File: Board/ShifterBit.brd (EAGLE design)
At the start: 27.2 x 51.2 mm, 10 parts

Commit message: renamed and added voltage divider for signal input
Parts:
- added R4: 2200, SparkFun-Passives:0603-RES
- added R5: 560, SparkFun-Passives:0603-RES
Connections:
- net A: now also R4.1, R5.2
- net GND: now also R5.1
- net SIG_IN: now also R4.2
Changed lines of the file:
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@@
 <element name="R2" library="SparkFun-Passives" package="0603-RES" value="56" x="9.3" y="50.8"/>
 <element name="R3" library="SparkFun-Passives" package="0603-RES" value="56" x="9.1" y="7.4"/>
+<element name="R4" library="SparkFun-Passives" package="0603-RES" value="2200" x="22.1" y="44.6"/>
+<element name="R5" library="SparkFun-Passives" package="0603-RES" value="560" x="18.4" y="44.6"/>
 </elements>
 <signals>
@@
 <contactref element="LED1" pad="C"/>
 <contactref element="LED2" pad="C"/>
+<contactref element="R5" pad="1"/>
 <wire x1="11.45" y1="53.13" x2="10.67" y2="56.835" width="0" layer="19" extent="16-16"/>
 <wire x1="14.177" y1="50.8" x2="11.45" y2="53.13" width="0" layer="19" extent="1-16"/>
@@
 <wire x1="6.5" y1="24.15" x2="6.6" y2="32.1" width="0" layer="19" extent="16-16"/>
 <wire x1="2.8" y1="17.77" x2="6.5" y2="24.15" width="0" layer="19" extent="16-16"/>
-<wire x1="13.777" y1="7.3" x2="2.8" y2="17.77" width="0" layer="19" extent="1-1"/>
+<wire x1="18.8" y1="22.25" x2="6.5" y2="24.15" width="0" layer="19" extent="16-16"/>
+<wire x1="23.2" y1="16.67" x2="18.8" y2="22.25" width="0" layer="19" extent="16-16"/>
+<wire x1="13.777" y1="7.3" x2="23.2" y2="16.67" width="0" layer="19" extent="1-1"/>
 <wire x1="10.67" y1="3.44" x2="13.777" y2="7.3" width="0" layer="19" extent="1-1"/>
-<wire x1="23.2" y1="16.67" x2="13.777" y2="7.3" width="0" layer="19" extent="1-1"/>
-<wire x1="18.8" y1="22.25" x2="23.2" y2="16.67" width="0" layer="19" extent="16-16"/>
+<wire x1="17.55" y1="44.6" x2="10.67" y2="3.44" width="0" layer="19" extent="1-1"/>
 </signal>
 <signal name="VCC">
@@
 <contactref element="BSM1" pad="SIG1"/>
 <contactref element="R1" pad="2"/>
+<contactref element="R4" pad="2"/>
 <wire x1="13.15" y1="53.13" x2="13.21" y2="56.835" width="0" layer="19" extent="16-16"/>
+<wire x1="22.95" y1="44.6" x2="13.15" y2="53.13" width="0" layer="19" extent="1-16"/>
 </signal>
 <signal name="RST">
@@
 <signal name="A">
 <contactref element="P1" pad="2"/>
+<contactref element="R5" pad="2"/>
+<contactref element="R4" pad="1"/>
+<wire x1="21.25" y1="44.6" x2="23.2" y2="36.99" width="0" layer="19" extent="1-1"/>
+<wire x1="19.25" y1="44.6" x2="21.25" y2="44.6" width="0" layer="19" extent="1-1"/>
 </signal>
 <signal name="EN">

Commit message: added transistor and some labels
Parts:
- added Q1: (no value), SparkFun-DiscreteSemi:TO-92-AMMO
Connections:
- new net N$14: Q1.3
- net D16: now also Q1.2
- net VCC: now also Q1.1
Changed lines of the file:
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@@
 <element name="R4" library="SparkFun-Passives" package="0603-RES" value="2200" x="22.1" y="44.6"/>
 <element name="R5" library="SparkFun-Passives" package="0603-RES" value="560" x="18.4" y="44.6"/>
+<element name="Q1" library="SparkFun-DiscreteSemi" package="TO-92-AMMO" value="" x="-0.4" y="-22.5"/>
 </elements>
 <signals>
@@
 <contactref element="BSM1" pad="VCC1"/>
 <contactref element="BSF1" pad="VCC"/>
+<contactref element="Q1" pad="1"/>
 <wire x1="15.75" y1="3.44" x2="15.75" y2="56.835" width="0" layer="19" extent="1-1"/>
+<wire x1="-2.94" y1="-22.5" x2="15.75" y2="3.44" width="0" layer="19" extent="1-1"/>
 </signal>
 <signal name="SIG_OUT">
@@
 <signal name="D16">
 <contactref element="P1" pad="4"/>
+<contactref element="Q1" pad="2"/>
+<wire x1="-0.4" y1="-22.5" x2="23.2" y2="31.91" width="0" layer="19" extent="1-1"/>
 </signal>
 <signal name="D14">
@@
 <wire x1="12.023" y1="7.3" x2="9.95" y2="7.4" width="0" layer="19" extent="1-1"/>
 </signal>
+<signal name="N$14">
+<contactref element="Q1" pad="3"/>
+</signal>
 </signals>

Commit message: added resistor to dac
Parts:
- added R6: 1200, SparkFun-Resistors:0603-RES
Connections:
- new net N$10: Q1.2, R6.2
- net D16: now also R6.1; no longer Q1.2
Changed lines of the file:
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@@
 <layer number="227" name="227bmp" color="7" fill="1" visible="yes" active="yes"/>
 <layer number="228" name="228bmp" color="7" fill="1" visible="yes" active="yes"/>
+<layer number="229" name="229bmp" color="7" fill="1" visible="yes" active="yes"/>
+<layer number="230" name="230bmp" color="7" fill="1" visible="yes" active="yes"/>
 <layer number="231" name="Eagle3D_PG1" color="7" fill="1" visible="no" active="no"/>
 <layer number="232" name="Eagle3D_PG2" color="7" fill="1" visible="no" active="no"/>
@@
 <element name="R5" library="SparkFun-Passives" package="0603-RES" value="560" x="18.4" y="44.6"/>
 <element name="Q1" library="SparkFun-DiscreteSemi" package="TO-92-AMMO" value="" x="-0.4" y="-22.5"/>
+<element name="R6" library="SparkFun-Resistors" package="0603-RES" value="1200" x="-2.4" y="-25.6"/>
 </elements>
 <signals>
@@
 <signal name="D16">
 <contactref element="P1" pad="4"/>
-<contactref element="Q1" pad="2"/>
-<wire x1="-0.4" y1="-22.5" x2="23.2" y2="31.91" width="0" layer="19" extent="1-1"/>
+<contactref element="R6" pad="1"/>
+<wire x1="-3.25" y1="-25.6" x2="23.2" y2="31.91" width="0" layer="19" extent="1-1"/>
 </signal>
 <signal name="D14">
@@
 <contactref element="Q1" pad="3"/>
 </signal>
+<signal name="N$10">
+<contactref element="R6" pad="2"/>
+<contactref element="Q1" pad="2"/>
+<wire x1="-0.4" y1="-22.5" x2="-1.55" y2="-25.6" width="0" layer="19" extent="1-1"/>
+</signal>
 </signals>

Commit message: connected the sd card
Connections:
- removed net N$1: SD1.5
- removed net N$11: SD1.2
- removed net N$12: SD1.1
- removed net N$2: SD1.3
- removed net N$3: SD1.4
- removed net N$5: SD1.6
- removed net N$6: SD1.7
- removed net N$7: SD1.8
- removed net N$8: SD1.11
- net 3V: now also SD1.4
- net D12: now also SD1.7
- net D13: now also SD1.3
- net D14: now also SD1.5
- net D15: now also SD1.2
- net GND: now also SD1.6
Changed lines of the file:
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@@
 <contactref element="LED2" pad="C"/>
 <contactref element="R5" pad="1"/>
+<contactref element="SD1" pad="6"/>
 <wire x1="11.45" y1="53.13" x2="10.67" y2="56.835" width="0" layer="19" extent="16-16"/>
 <wire x1="14.177" y1="50.8" x2="11.45" y2="53.13" width="0" layer="19" extent="1-16"/>
-<wire x1="18.8" y1="35.6" x2="14.177" y2="50.8" width="0" layer="19" extent="1-16"/>
-<wire x1="6.6" y1="32.1" x2="18.8" y2="35.6" width="0" layer="19" extent="16-16"/>
-<wire x1="6.5" y1="24.15" x2="6.6" y2="32.1" width="0" layer="19" extent="16-16"/>
+<wire x1="17.55" y1="44.6" x2="14.177" y2="50.8" width="0" layer="19" extent="1-1"/>
+<wire x1="18.8" y1="35.6" x2="17.55" y2="44.6" width="0" layer="19" extent="1-16"/>
+<wire x1="19.3" y1="31.3" x2="18.8" y2="35.6" width="0" layer="19" extent="16-16"/>
+<wire x1="18.8" y1="22.25" x2="19.3" y2="31.3" width="0" layer="19" extent="16-16"/>
+<wire x1="23.2" y1="16.67" x2="18.8" y2="22.25" width="0" layer="19" extent="16-16"/>
+<wire x1="6.5" y1="24.15" x2="18.8" y2="22.25" width="0" layer="19" extent="16-16"/>
 <wire x1="2.8" y1="17.77" x2="6.5" y2="24.15" width="0" layer="19" extent="16-16"/>
-<wire x1="18.8" y1="22.25" x2="6.5" y2="24.15" width="0" layer="19" extent="16-16"/>
-<wire x1="23.2" y1="16.67" x2="18.8" y2="22.25" width="0" layer="19" extent="16-16"/>
+<wire x1="6.6" y1="32.1" x2="6.5" y2="24.15" width="0" layer="19" extent="16-16"/>
 <wire x1="13.777" y1="7.3" x2="23.2" y2="16.67" width="0" layer="19" extent="1-1"/>
 <wire x1="10.67" y1="3.44" x2="13.777" y2="7.3" width="0" layer="19" extent="1-1"/>
-<wire x1="17.55" y1="44.6" x2="10.67" y2="3.44" width="0" layer="19" extent="1-1"/>
 </signal>
 <signal name="VCC">
@@
 <signal name="D14">
 <contactref element="P1" pad="5"/>
+<contactref element="SD1" pad="5"/>
+<wire x1="19.3" y1="30.2" x2="23.2" y2="29.37" width="0" layer="19" extent="16-16"/>
 </signal>
 <signal name="D12">
 <contactref element="P1" pad="6"/>
+<contactref element="SD1" pad="7"/>
+<wire x1="19.3" y1="32.4" x2="23.2" y2="26.83" width="0" layer="19" extent="16-16"/>
 </signal>
 <signal name="D13">
 <contactref element="P1" pad="7"/>
+<contactref element="SD1" pad="3"/>
+<wire x1="19.3" y1="28" x2="23.2" y2="24.29" width="0" layer="19" extent="16-16"/>
 </signal>
 <signal name="V+">
@@
 <signal name="D15">
 <contactref element="P2" pad="4"/>
+<contactref element="SD1" pad="2"/>
+<wire x1="2.8" y1="25.39" x2="19.3" y2="26.9" width="0" layer="19" extent="16-16"/>
 </signal>
 <signal name="3V">
 <contactref element="P2" pad="3"/>
+<contactref element="SD1" pad="4"/>
+<wire x1="2.8" y1="22.85" x2="19.3" y2="29.1" width="0" layer="19" extent="16-16"/>
 </signal>
 <signal name="LD0">
 <contactref element="P2" pad="2"/>
 </signal>
-<signal name="N$1">
-<contactref element="SD1" pad="5"/>
-</signal>
-<signal name="N$2">
-<contactref element="SD1" pad="3"/>
-</signal>
-<signal name="N$3">
-<contactref element="SD1" pad="4"/>
-</signal>
-<signal name="N$5">
-<contactref element="SD1" pad="6"/>
-</signal>
-<signal name="N$6">
-<contactref element="SD1" pad="7"/>
-</signal>
-<signal name="N$7">
-<contactref element="SD1" pad="8"/>
-</signal>
-<signal name="N$8">
-<contactref element="SD1" pad="11"/>
-</signal>
-<signal name="N$11">
-<contactref element="SD1" pad="2"/>
-</signal>
-<signal name="N$12">
-<contactref element="SD1" pad="1"/>
-</signal>
 <signal name="N$4">

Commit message: changed resistor name
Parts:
- R6: value 1200 -> 1K2
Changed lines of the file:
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@@
 <element name="R5" library="SparkFun-Passives" package="0603-RES" value="560" x="18.4" y="44.6"/>
 <element name="Q1" library="SparkFun-DiscreteSemi" package="TO-92-AMMO" value="" x="-0.4" y="-22.5"/>
-<element name="R6" library="SparkFun-Resistors" package="0603-RES" value="1200" x="-2.4" y="-25.6"/>
+<element name="R6" library="SparkFun-Resistors" package="0603-RES" value="1K2" x="-2.4" y="-25.6"/>
 </elements>
 <signals>

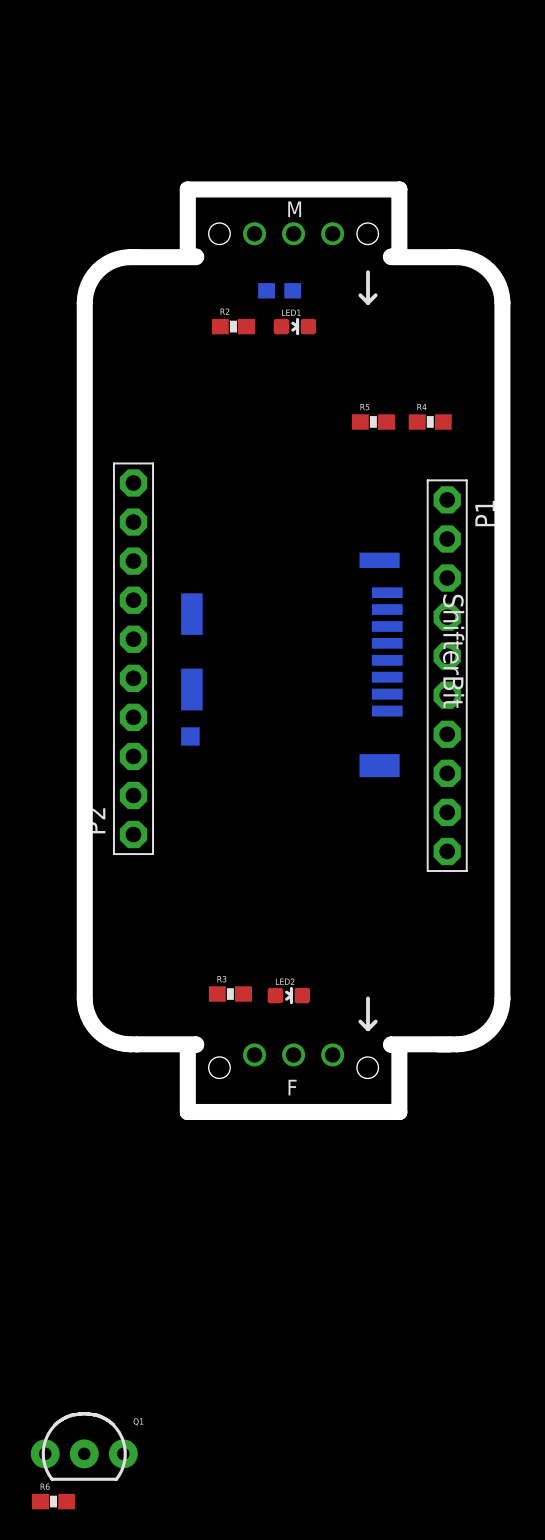
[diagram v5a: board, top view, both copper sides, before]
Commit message: added component to board
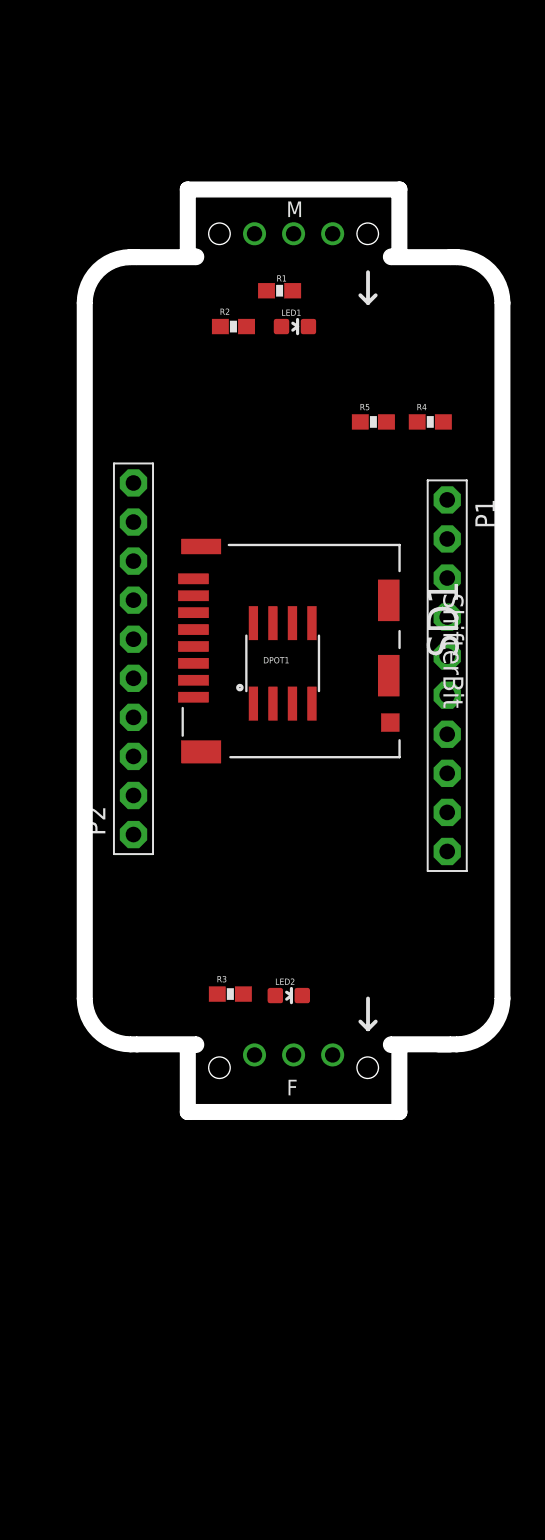
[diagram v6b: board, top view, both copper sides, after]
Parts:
- removed Q1: (no value), SparkFun-DiscreteSemi:TO-92-AMMO
- removed R6: 1K2, SparkFun-Resistors:0603-RES
- added DPOT1: MCP41XXX, SparkFun-AnalogIC:SO08
- R4: value 2200 -> 2K2
- moved SD1 12.6 mm to (6.70, 26.7), flipped to the top
- flipped R1 to the top
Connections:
- removed net N$10: Q1.2, R6.2
- removed net N$14: Q1.3
- net 3V: now also DPOT1.8
- net D13: now also DPOT1.3
- net D14: now also DPOT1.2
- net D16: now also DPOT1.1; no longer R6.1
- net GND: now also DPOT1.4, DPOT1.7
- net SIG_OUT: now also DPOT1.6
- net VCC: now also DPOT1.5; no longer Q1.1

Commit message: made board longer and placed all components on top
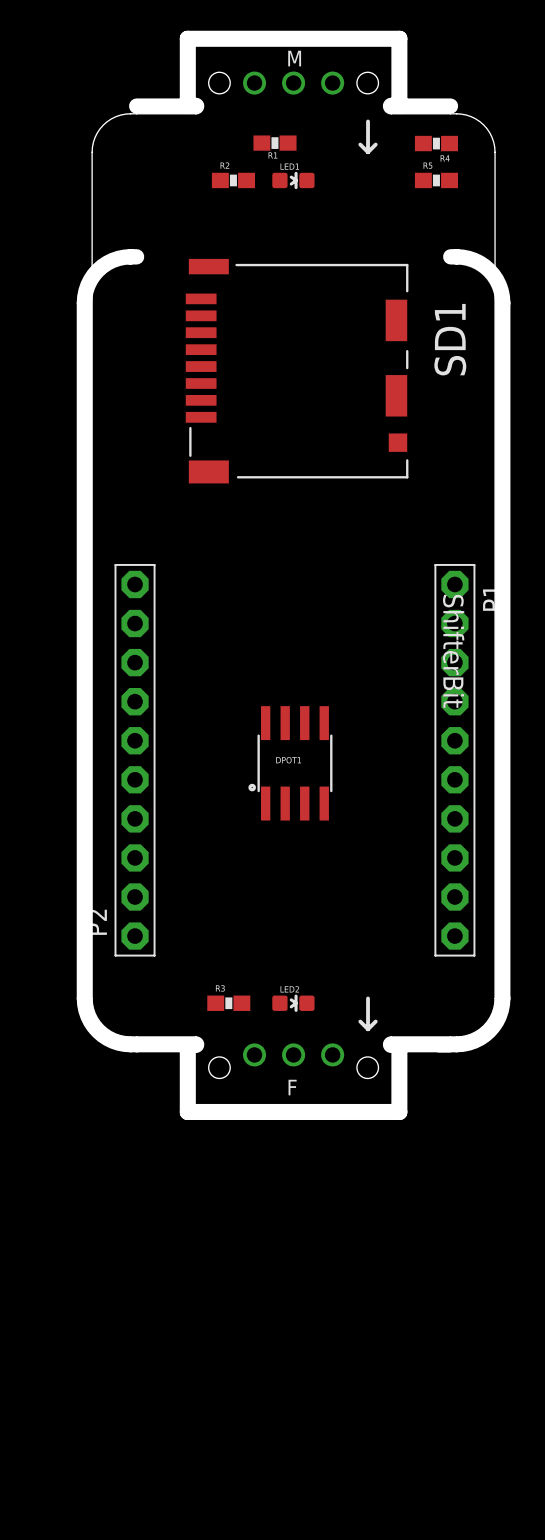
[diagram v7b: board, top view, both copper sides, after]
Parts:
- moved SD1 18.2 mm to (7.20, 44.9)
- moved R4 18.1 mm to (22.5, 62.7), turned to 180 degrees
- moved R5 16.2 mm to (22.5, 60.3)
- moved BSM1 9.80 mm to (19.8, 69.2)
- moved R1 9.60 mm to (12.0, 62.7), turned to 0 degrees
- moved LED1 9.50 mm to (13.2, 60.3)
- moved R2 9.50 mm to (9.30, 60.3)
- moved P2 6.60 mm to (2.90, 22.6)
- moved DPOT1 6.55 mm to (13.3, 22.4)
- moved P1 5.52 mm to (23.7, 22.6)
- moved R3 0.61 mm to (9.00, 6.80)
- moved LED2 0.58 mm to (13.2, 6.80)
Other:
- board size 27.2 x 51.2 mm -> 27.2 x 60.5 mm
